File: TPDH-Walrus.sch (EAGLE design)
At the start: 44 parts, among them Q2 DMG3404, U1 MS5803-14BA, U2 SN65HVD33RHL, U4 MCP3421A3, U5 TPS79733, U6 MAX6070AAUT18, U7 TXS0102DQM

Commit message: Update +3V3 symbol and re-route
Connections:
- removed net 3V3: C1.1, C10.1, C3.1, C5.1, C8.1, C9.1, ISP1.VCC, JP1.1, R1.2, R2.2, R3.2, R5.2, U1.PS, U1.VDD, U2.VCC, U3.VCC, U4.VDD, U5.VOUT, U6.VIN, U7.EN, U7.VA
- new net +3V3: C1.1, C10.1, C3.1, C5.1, C8.1, C9.1, ISP1.VCC, JP1.1, R1.2, R2.2, R3.2, R5.2, THERM.2, U1.PS, U1.VDD, U2.VCC, U3.VCC, U4.VDD, U5.VOUT, U6.VIN, U7.EN, U7.VA
- net VREF: no longer THERM.2
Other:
- note removed: "Extra things to attach to MCU"

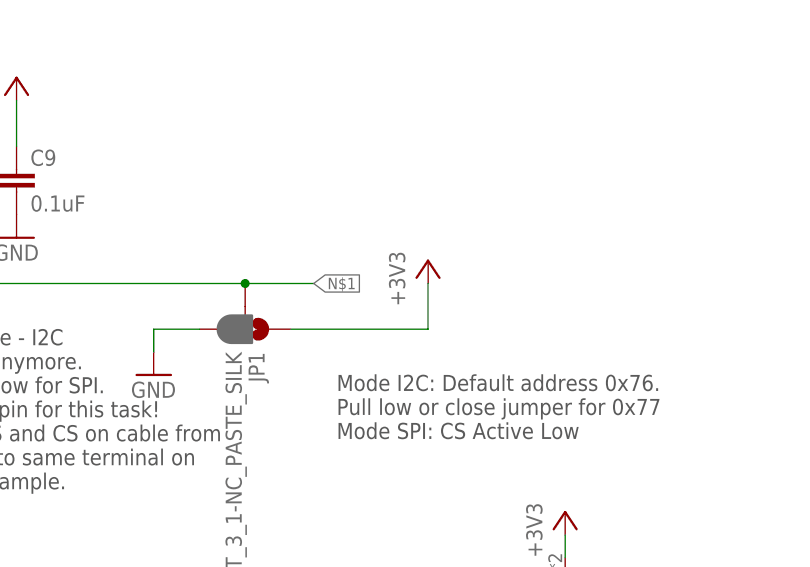
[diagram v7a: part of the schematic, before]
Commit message: Name SPI-I2C switch
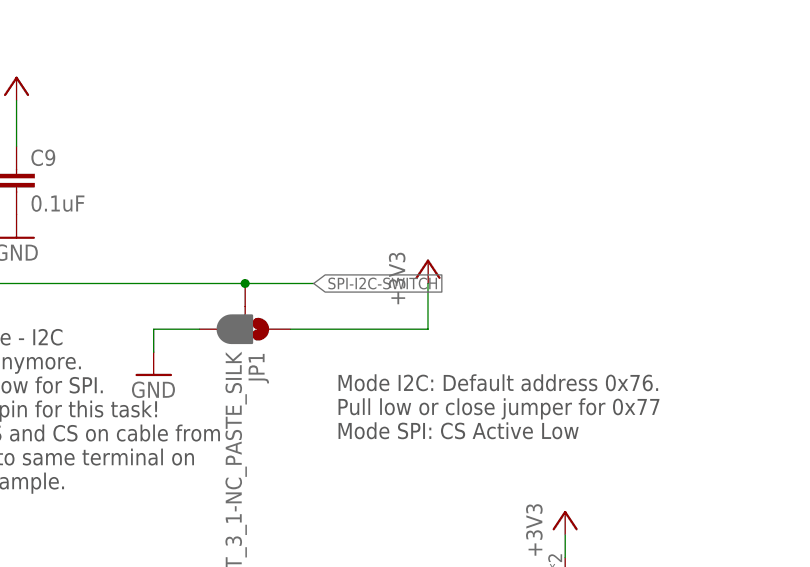
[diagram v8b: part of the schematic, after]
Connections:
- net N$1 renamed SPI-I2C-SWITCH
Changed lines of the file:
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@@
 </segment>
 </net>
-<net name="N$1" class="0">
+<net name="SPI-I2C-SWITCH" class="0">
 <segment>
 <pinref part="U1" gate="G$1" pin="AD/CS"/>
